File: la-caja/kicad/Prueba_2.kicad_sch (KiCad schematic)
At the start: 1 part

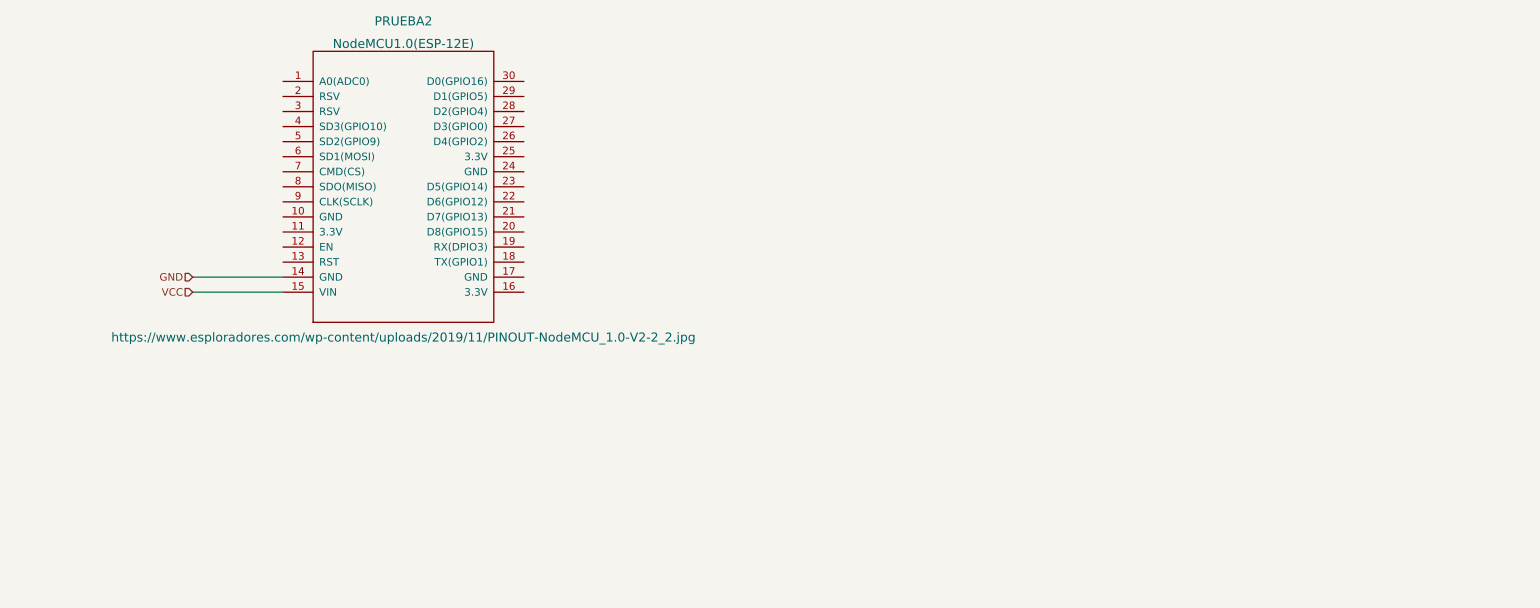
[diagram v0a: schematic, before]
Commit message: Esquematico actualizado, nuevo símbolo para numpad
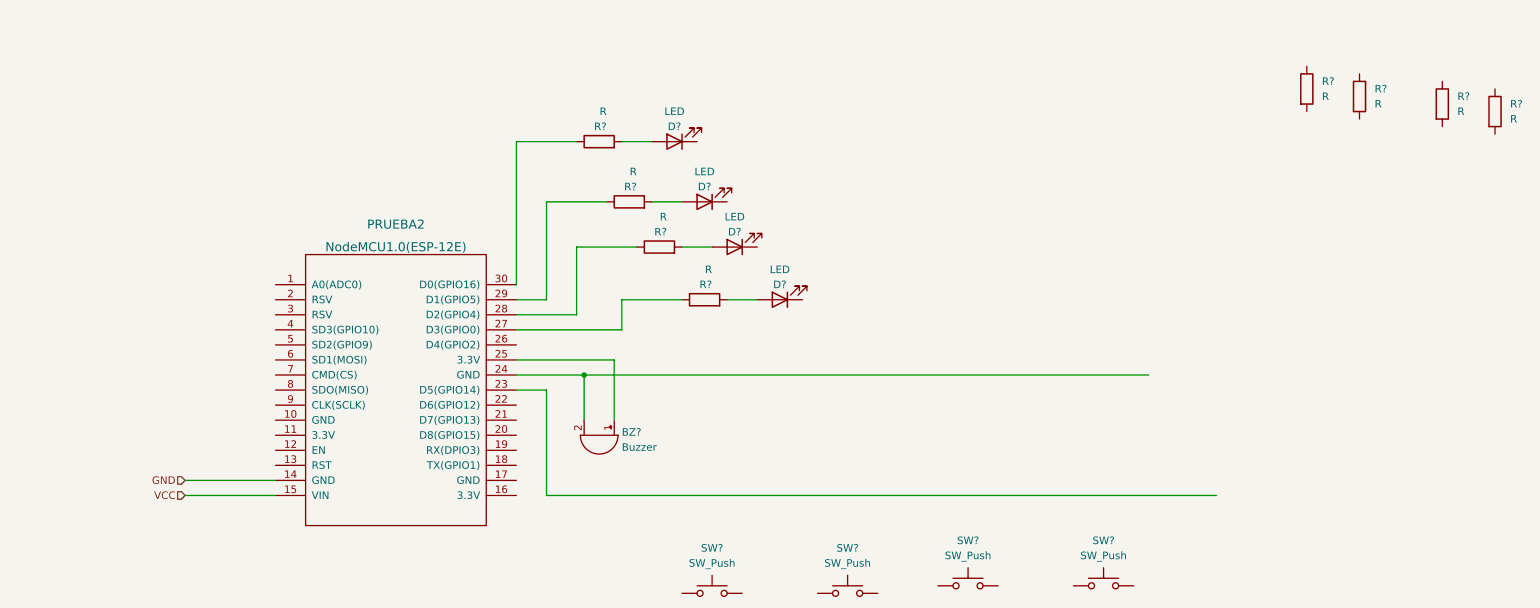
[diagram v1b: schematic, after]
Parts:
- added BZ?: Buzzer, symbol Device:Buzzer
- added D? (x4): LED, symbol Device:LED
- added R? (x8): R, symbol Device:R
- added SW? (x4): SW_Push, symbol Switch:SW_Push
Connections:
- net at PRUEBA2.24 (GND): now also BZ?.2 (+)
- net at PRUEBA2.25 (3.3V): now also BZ?.1 (-)
- net at PRUEBA2.27 (D3(GPIO0)): now also R?.1
- net at PRUEBA2.28 (D2(GPIO4)): now also R?.1
- net at PRUEBA2.29 (D1(GPIO5)): now also R?.1
- net at PRUEBA2.30 (D0(GPIO16)): now also R?.1
- new net: D?.2 (A), R?.2 (x4)
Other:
- moved on the sheet: PRUEBA2
